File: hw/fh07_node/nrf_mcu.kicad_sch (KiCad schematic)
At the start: 2 parts, among them J1 Conn_ARM_JTAG_SWD_10, M1 ME54BS01_V1.0

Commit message: Add ME54BS01 power filtering and decoupling
- Added ferrite bead between VCC and VCCM_nRF
- Added 0.1uF + 4.7uF decoupling on module supply
- Confirmed SWD connectivity and GPIO availability
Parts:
- added C1: 0.1 uF, symbol Device:C
- added C2: 4.7 uF, symbol Device:C
- added D1: LED, symbol Device:LED
- added FB1: FerriteBead, symbol Device:FerriteBead
- added R1: 2.2 kΩ, symbol Device:R
- renumbered J1 to J?, M1 to M?
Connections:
- net GND: now also C1.2, C2.2, D1.1 (K)
- net VCC: now also FB1.1; no longer M?.14 (VCCM_nRF)
- net LED_STAT: now reaches M?.23 (P0.00)
- net LED_STAT: now also R1.1
- new net: D1.2 (A), R1.2
- new net VCCM_nRF: C1.1, C2.1, FB1.2, M?.14 (VCCM_nRF)
- no-connect marks 16 -> 15

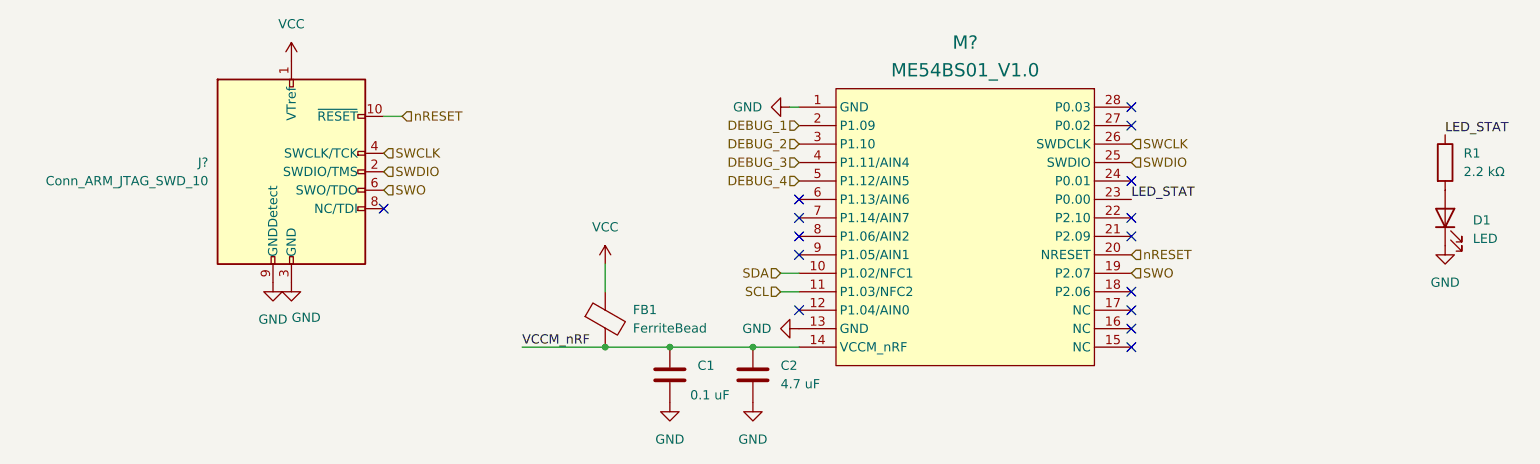
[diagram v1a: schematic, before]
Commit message: Updated sensor node and top level sheet
Fixed pin naming on sensor module and update MCU and Sensor top sheet
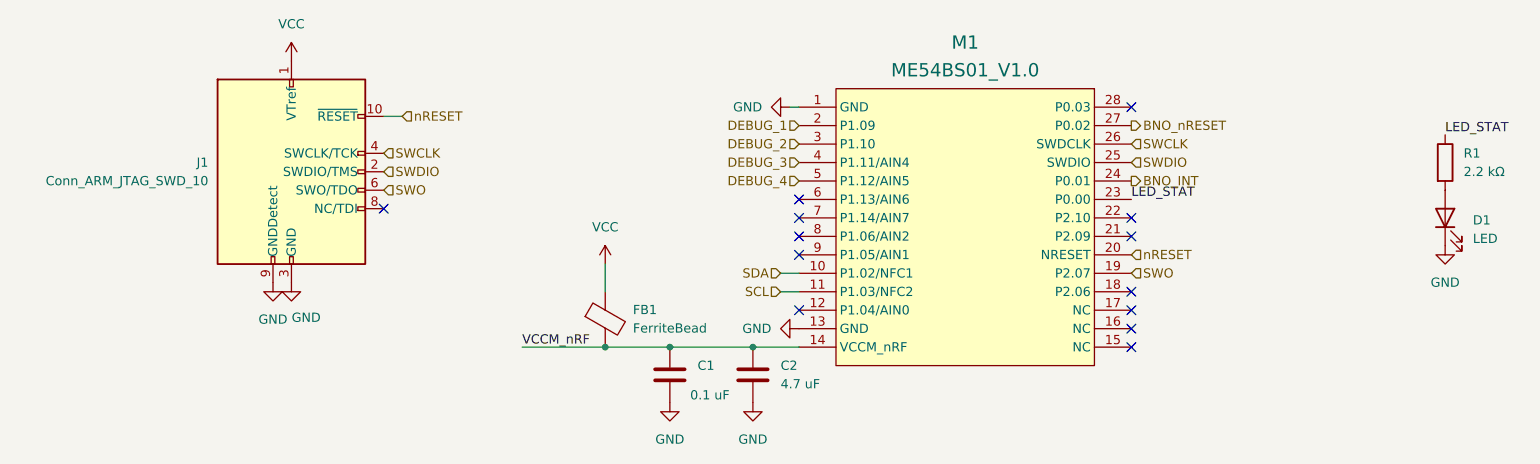
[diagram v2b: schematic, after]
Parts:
- gave numbers to parts that had none: 2
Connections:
- net BNO_INT: now reaches M1.24 (P0.01)
- net BNO_nRESET: now reaches M1.27 (P0.02)
- no-connect marks 15 -> 13
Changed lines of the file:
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@@
-	)
-	(no_connect
-		(at 177.8 69.85)
 	)
 	(no_connect
 		(at 132.08 80.01)
-	)
-	(no_connect
-		(at 177.8 77.47)
 	)
 	(no_connect
@@
 		)
 	)
+	(hierarchical_label "BNO_nRESET"
+		(shape output)
+		(at 177.8 69.85 0)
+		(effects
+			(font
+				(size 1.27 1.27)
+			)
+			(justify left)
+		)
+	)
 	(hierarchical_label "SCL"
 		(shape input)
@@
 		)
 	)
+	(hierarchical_label "BNO_INT"
+		(shape output)
+		(at 177.8 77.47 0)
+		(effects
+			(font
+				(size 1.27 1.27)
+			)
+			(justify left)
+		)
+	)
 	(hierarchical_label "DEBUG_4"
 		(shape input)
@@
 		(dnp no)
 		(fields_autoplaced yes)
-		(property "Reference" "#PWR03"
+		(property "Reference" "#PWR?"
 			(at 114.3 114.3 0)
 			(effects
@@
 				)
 			)
+			(project "fh07_node"
+				(path "/aea54c0a-0593-4c80-97cc-583e63973e87/d389981d-ba8e-4d67-beea-f26bc49c75ef"
+					(reference "#PWR?")
+					(unit 1)
+				)
+			)
 		)
 	)
@@
 		(dnp no)
 		(fields_autoplaced yes)
-		(property "Reference" "J?"
+		(property "Reference" "J1"
 			(at 50.8 74.9299 0)
 			(effects
@@
 		(on_board yes)
 		(dnp no)
-		(property "Reference" "#PWR?"
+		(property "Reference" "#PWR08"
 			(at 62.23 97.79 0)
 			(effects
@@
 		(dnp no)
 		(fields_autoplaced yes)
-		(property "Reference" "#PWR04"
+		(property "Reference" "#PWR?"
 			(at 220.98 92.71 0)
 			(effects
@@
 				)
 			)
+			(project "fh07_node"
+				(path "/aea54c0a-0593-4c80-97cc-583e63973e87/d389981d-ba8e-4d67-beea-f26bc49c75ef"
+					(reference "#PWR?")
+					(unit 1)
+				)
+			)
 		)
 	)
@@
 		(dnp no)
 		(fields_autoplaced yes)
-		(property "Reference" "#PWR01"
+		(property "Reference" "#PWR?"
 			(at 105.41 92.71 0)
 			(effects
@@
 				)
 			)
+			(project "fh07_node"
+				(path "/aea54c0a-0593-4c80-97cc-583e63973e87/d389981d-ba8e-4d67-beea-f26bc49c75ef"
+					(reference "#PWR?")
+					(unit 1)
+				)
+			)
 		)
 	)
@@
 		(dnp no)
 		(fields_autoplaced yes)
-		(property "Reference" "#PWR?"
+		(property "Reference" "#PWR07"
 			(at 59.69 97.79 0)
 			(effects
@@
 		(dnp no)
 		(fields_autoplaced yes)
-		(property "Reference" "FB1"
+		(property "Reference" "FB?"
 			(at 109.22 95.1991 0)
 			(effects
@@
 				)
 			)
+			(project "fh07_node"
+				(path "/aea54c0a-0593-4c80-97cc-583e63973e87/d389981d-ba8e-4d67-beea-f26bc49c75ef"
+					(reference "FB?")
+					(unit 1)
+				)
+			)
 		)
 	)
@@
 		(dnp no)
 		(fields_autoplaced yes)
-		(property "Reference" "C2"
+		(property "Reference" "C?"
 			(at 129.54 102.8699 0)
 			(effects
@@
 				)
 			)
+			(project "fh07_node"
+				(path "/aea54c0a-0593-4c80-97cc-583e63973e87/d389981d-ba8e-4d67-beea-f26bc49c75ef"
+					(reference "C?")
+					(unit 1)
+				)
+			)
 		)
 	)
@@
 		(dnp no)
 		(fields_autoplaced yes)
-		(property "Reference" "M?"
+		(property "Reference" "M1"
 			(at 154.94 58.42 0)
 			(effects
@@
 		(dnp no)
 		(fields_autoplaced yes)
-		(property "Reference" "#PWR?"
+		(property "Reference" "#PWR05"
 			(at 62.23 64.77 0)
 			(effects
@@
 		(dnp no)
 		(fields_autoplaced yes)
-		(property "Reference" "D1"
+		(property "Reference" "D?"
 			(at 224.79 82.8674 90)
 			(effects
@@
 				)
 			)
+			(project "fh07_node"
+				(path "/aea54c0a-0593-4c80-97cc-583e63973e87/d389981d-ba8e-4d67-beea-f26bc49c75ef"
+					(reference "D?")
+					(unit 1)
+				)
+			)
 		)
 	)
@@
 		(dnp no)
 		(fields_autoplaced yes)
-		(property "Reference" "#PWR02"
+		(property "Reference" "#PWR?"
 			(at 125.73 114.3 0)
 			(effects
@@
 				)
 			)
+			(project "fh07_node"
+				(path "/aea54c0a-0593-4c80-97cc-583e63973e87/d389981d-ba8e-4d67-beea-f26bc49c75ef"
+					(reference "#PWR?")
+					(unit 1)
+				)
+			)
 		)
 	)
@@
 		(dnp no)
 		(fields_autoplaced yes)
-		(property "Reference" "#PWR?"
+		(property "Reference" "#PWR03"
 			(at 125.73 97.79 0)
 			(effects
@@
 		(on_board yes)
 		(dnp no)
-		(property "Reference" "C1"
+		(property "Reference" "C?"
 			(at 118.11 102.8699 0)
 			(effects
@@
 				)
 			)
+			(project "fh07_node"
+				(path "/aea54c0a-0593-4c80-97cc-583e63973e87/d389981d-ba8e-4d67-beea-f26bc49c75ef"
+					(reference "C?")
+					(unit 1)
+				)
+			)
 		)
 	)
@@
 		(dnp no)
 		(fields_autoplaced yes)
-		(property "Reference" "#PWR?"
+		(property "Reference" "#PWR04"
 			(at 124.46 67.31 0)
 			(effects
@@
 		(dnp no)
 		(fields_autoplaced yes)
-		(property "Reference" "R1"
+		(property "Reference" "R?"
 			(at 223.52 73.6599 0)
 			(effects
@@
 					(unit 1)
 				)
+			)
+			(project "fh07_node"
+				(path "/aea54c0a-0593-4c80-97cc-583e63973e87/d389981d-ba8e-4d67-beea-f26bc49c75ef"
+					(reference "R?")
+					(unit 1)
+				)

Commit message: Completed hardware revision 1 release
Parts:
- C8: renamed from C1; footprint (none) -> Capacitor_SMD:C_1206_3216Metric_Pad1.33x1.80mm_HandSolder
- C9: renamed from C2; footprint (none) -> Capacitor_SMD:C_1206_3216Metric_Pad1.33x1.80mm_HandSolder
- D1, FB1: footprint (none) -> Diode_SMD:D_1206_3216Metric_Pad1.42x1.75mm_HandSolder
- R1: footprint (none) -> Resistor_SMD:R_1206_3216Metric_Pad1.30x1.75mm_HandSolder
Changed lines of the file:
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@@
 		(dnp no)
 		(fields_autoplaced yes)
-		(property "Reference" "#PWR?"
+		(property "Reference" "#PWR0102"
 			(at 114.3 114.3 0)
 			(effects
@@
 			(project "fh07_node"
 				(path "/aea54c0a-0593-4c80-97cc-583e63973e87/d389981d-ba8e-4d67-beea-f26bc49c75ef"
-					(reference "#PWR?")
+					(reference "#PWR0102")
 					(unit 1)
 				)
@@
 		(dnp no)
 		(fields_autoplaced yes)
-		(property "Reference" "#PWR?"
+		(property "Reference" "#PWR0105"
 			(at 220.98 92.71 0)
 			(effects
@@
 			(project "fh07_node"
 				(path "/aea54c0a-0593-4c80-97cc-583e63973e87/d389981d-ba8e-4d67-beea-f26bc49c75ef"
-					(reference "#PWR?")
+					(reference "#PWR0105")
 					(unit 1)
 				)
@@
 		(dnp no)
 		(fields_autoplaced yes)
-		(property "Reference" "#PWR?"
+		(property "Reference" "#PWR0104"
 			(at 105.41 92.71 0)
 			(effects
@@
 			(project "fh07_node"
 				(path "/aea54c0a-0593-4c80-97cc-583e63973e87/d389981d-ba8e-4d67-beea-f26bc49c75ef"
-					(reference "#PWR?")
+					(reference "#PWR0104")
 					(unit 1)
 				)
@@
 		(dnp no)
 		(fields_autoplaced yes)
-		(property "Reference" "FB?"
+		(property "Reference" "FB1"
 			(at 109.22 95.1991 0)
 			(effects
@@
 			)
 		)
-		(property "Footprint" ""
+		(property "Footprint" "Diode_SMD:D_1206_3216Metric_Pad1.42x1.75mm_HandSolder"
 			(at 103.632 96.52 90)
 			(effects
@@
 			(project "fh07_node"
 				(path "/aea54c0a-0593-4c80-97cc-583e63973e87/d389981d-ba8e-4d67-beea-f26bc49c75ef"
-					(reference "FB?")
+					(reference "FB1")
 					(unit 1)
 				)
@@
 		(dnp no)
 		(fields_autoplaced yes)
-		(property "Reference" "C?"
+		(property "Reference" "C9"
 			(at 129.54 102.8699 0)
 			(effects
@@
 			)
 		)
-		(property "Footprint" ""
+		(property "Footprint" "Capacitor_SMD:C_1206_3216Metric_Pad1.33x1.80mm_HandSolder"
 			(at 126.6952 107.95 0)
 			(effects
@@
 			(project "fh07_node"
 				(path "/aea54c0a-0593-4c80-97cc-583e63973e87/d389981d-ba8e-4d67-beea-f26bc49c75ef"
-					(reference "C?")
+					(reference "C9")
 					(unit 1)
 				)
@@
 		(dnp no)
 		(fields_autoplaced yes)
-		(property "Reference" "D?"
+		(property "Reference" "D1"
 			(at 224.79 82.8674 90)
 			(effects
@@
 			)
 		)
-		(property "Footprint" ""
+		(property "Footprint" "Diode_SMD:D_1206_3216Metric_Pad1.42x1.75mm_HandSolder"
 			(at 220.98 82.55 0)
 			(effects
@@
 			(project "fh07_node"
 				(path "/aea54c0a-0593-4c80-97cc-583e63973e87/d389981d-ba8e-4d67-beea-f26bc49c75ef"
-					(reference "D?")
+					(reference "D1")
 					(unit 1)
 				)
@@
 		(dnp no)
 		(fields_autoplaced yes)
-		(property "Reference" "#PWR?"
+		(property "Reference" "#PWR0103"
 			(at 125.73 114.3 0)
 			(effects
@@
 			(project "fh07_node"
 				(path "/aea54c0a-0593-4c80-97cc-583e63973e87/d389981d-ba8e-4d67-beea-f26bc49c75ef"
-					(reference "#PWR?")
+					(reference "#PWR0103")
 					(unit 1)
 				)
@@
 		(on_board yes)
 		(dnp no)
-		(property "Reference" "C?"
+		(property "Reference" "C8"
 			(at 118.11 102.8699 0)
 			(effects
@@
 			)
 		)
-		(property "Footprint" ""
+		(property "Footprint" "Capacitor_SMD:C_1206_3216Metric_Pad1.33x1.80mm_HandSolder"
 			(at 115.2652 107.95 0)
 			(effects
@@
 			(project "fh07_node"
 				(path "/aea54c0a-0593-4c80-97cc-583e63973e87/d389981d-ba8e-4d67-beea-f26bc49c75ef"
-					(reference "C?")
+					(reference "C8")
 					(unit 1)
 				)
@@
 		(dnp no)
 		(fields_autoplaced yes)
-		(property "Reference" "R?"
+		(property "Reference" "R1"
 			(at 223.52 73.6599 0)
 			(effects
@@
 			)
 		)
-		(property "Footprint" ""
+		(property "Footprint" "Resistor_SMD:R_1206_3216Metric_Pad1.30x1.75mm_HandSolder"
 			(at 219.202 74.93 90)
 			(effects
@@
 			(project "fh07_node"
 				(path "/aea54c0a-0593-4c80-97cc-583e63973e87/d389981d-ba8e-4d67-beea-f26bc49c75ef"
-					(reference "R?")
-					(unit 1)
-				)
+					(reference "R1")
+					(unit 1)
+				)
